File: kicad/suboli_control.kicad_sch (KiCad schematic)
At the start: 37 parts, among them SW1 DPST power switch panel header

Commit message: Review fixes R1: annotation, final values, TVS populated (SMBJ20A)
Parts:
- C11: value 220-470 uF / 25 V L output coupling -> 470uF/25V L output coupling
- C12: value 220-470 uF / 25 V R output coupling -> 470uF/25V R output coupling
- J1: renamed from J_DC; Function (none) -> DC barrel jack 5.5x2.5
- J2: renamed from J_IN; Function (none) -> 3.5 mm TRS input jack
- J3: renamed from J_SPK; Function (none) -> 4-pole Speakon/XLR tactile output
- J4: renamed from J_HP; Function (none) -> 3.5 mm TRS headphone output jack
- R2: value 47-100 k L input bias to VGND -> 100k L input bias to VGND
- R3: value 47-100 k R input bias to VGND -> 100k R input bias to VGND
- RV1: renamed from P_TACT; Function (none) -> Tactile volume, dual-gang 10k log
- RV2: renamed from P_HP; Function (none) -> Headphone volume, dual-gang 10k log
- TVS1: value SMBJ24A TVS -> SMBJ20A TVS; now fitted
- U1: renamed from U_vg; Function (none) -> Virtual ground rail splitter
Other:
- note added: "Headphone output is AC-coupled: J4 sleeve connects to GND_SIG, not VGND."
- note removed: "Headphone output is AC-coupled: J_HP sleeve connects to GND_SIG, not VGND."

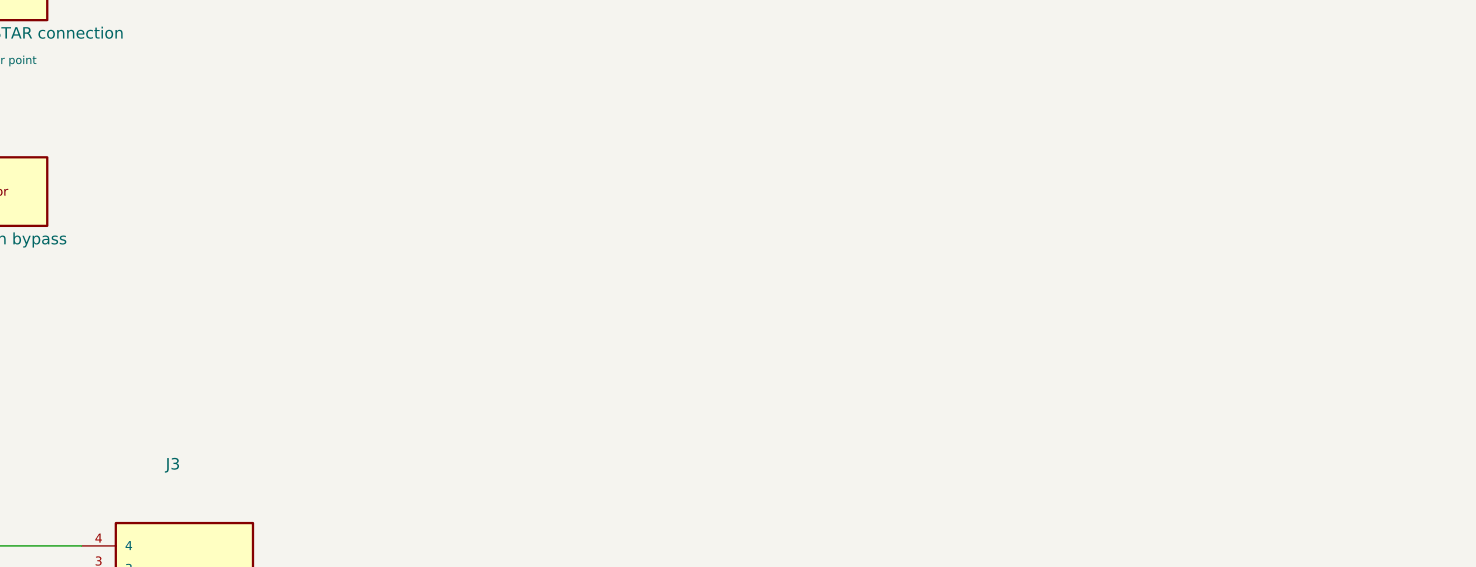
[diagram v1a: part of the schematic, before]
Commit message: R2: interior glow circuit, power-tracked via SW1
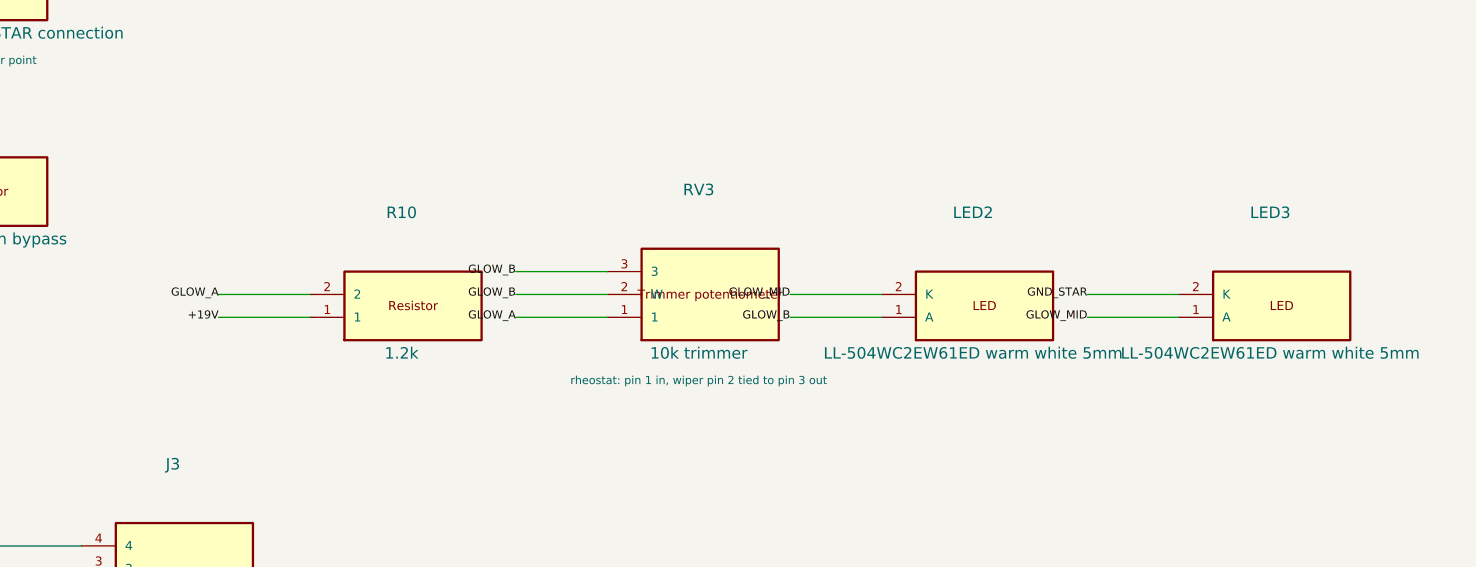
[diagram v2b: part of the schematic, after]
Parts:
- added LED2, LED3: LL-504WC2EW61ED warm white 5mm, symbol suboli_control:LED_2PIN
- added R10: 1.2k, symbol suboli_control:R_2PIN
- added RV3: 10k trimmer, symbol suboli_control:POT_3PIN
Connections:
- net +19V: now also R10.1
- net GND_STAR: now also LED3.2 (K)
- new net GLOW_A: R10.2, RV3.1
- new net GLOW_B: LED2.1 (A), RV3.2 (W), RV3.3
- new net GLOW_MID: LED2.2 (K), LED3.1 (A)
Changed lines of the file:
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@@
   (label "+19V_HP" (at 182.88 55.88 0) (effects (font (size 0.90 0.90)) (justify right)))
+  (symbol
+    (lib_id "suboli_control:R_2PIN")
+    (at 317.50 71.12 0)
+    (unit 1)
+    (exclude_from_sim no)
+    (in_bom yes)
+    (on_board yes)
+    (dnp no)
+    (property "Reference" "R10" (at 317.50 59.50 0) (effects (font (size 1.27 1.27))))
+    (property "Value" "1.2k" (at 317.50 75.12 0) (effects (font (size 1.27 1.27))))
+    (property "Footprint" "" (at 317.50 71.12 0) (effects (font (size 1.27 1.27)) (hide yes)))
+    (property "Datasheet" "~" (at 317.50 71.12 0) (effects (font (size 1.27 1.27)) (hide yes)))
+    (property "Function" "Glow current limit" (at 317.50 71.12 0) (effects (font (size 1.27 1.27)) (hide yes)))
+    (pin "1")
+    (pin "2")
+    (instances
+      (project "suboli_control"
+        (path "/35397207-27a9-5c6b-ad79-7b20c8370a7e"
+          (reference "R10")
+          (unit 1)
+        )
+      )
+    )
+  )
+  (wire (pts (xy 307.34 71.12) (xy 297.18 71.12)) (stroke (width 0) (type default)))
+  (label "+19V" (at 297.18 71.12 0) (effects (font (size 0.90 0.90)) (justify right)))
+  (wire (pts (xy 307.34 68.58) (xy 297.18 68.58)) (stroke (width 0) (type default)))
+  (label "GLOW_A" (at 297.18 68.58 0) (effects (font (size 0.90 0.90)) (justify right)))
+  (symbol
+    (lib_id "suboli_control:POT_3PIN")
+    (at 350.52 71.12 0)
+    (unit 1)
+    (exclude_from_sim no)
+    (in_bom yes)
+    (on_board yes)
+    (dnp no)
+    (property "Reference" "RV3" (at 350.52 56.96 0) (effects (font (size 1.27 1.27))))
+    (property "Value" "10k trimmer" (at 350.52 75.12 0) (effects (font (size 1.27 1.27))))
+    (property "Footprint" "" (at 350.52 71.12 0) (effects (font (size 1.27 1.27)) (hide yes)))
+    (property "Datasheet" "~" (at 350.52 71.12 0) (effects (font (size 1.27 1.27)) (hide yes)))
+    (property "Function" "Glow brightness set" (at 350.52 71.12 0) (effects (font (size 1.27 1.27)) (hide yes)))
+    (property "Wiring" "rheostat: pin 1 in, wiper pin 2 tied to pin 3 out" (at 350.52 78.12 0) (effects (font (size 0.90 0.90))))
+    (pin "1")
+    (pin "2")
+    (pin "3")
+    (instances
+      (project "suboli_control"
+        (path "/35397207-27a9-5c6b-ad79-7b20c8370a7e"
+          (reference "RV3")
+          (unit 1)
+        )
+      )
+    )
+  )
+  (wire (pts (xy 340.36 71.12) (xy 330.20 71.12)) (stroke (width 0) (type default)))
+  (label "GLOW_A" (at 330.20 71.12 0) (effects (font (size 0.90 0.90)) (justify right)))
+  (wire (pts (xy 340.36 68.58) (xy 330.20 68.58)) (stroke (width 0) (type default)))
+  (label "GLOW_B" (at 330.20 68.58 0) (effects (font (size 0.90 0.90)) (justify right)))
+  (wire (pts (xy 340.36 66.04) (xy 330.20 66.04)) (stroke (width 0) (type default)))
+  (label "GLOW_B" (at 330.20 66.04 0) (effects (font (size 0.90 0.90)) (justify right)))
+  (symbol
+    (lib_id "suboli_control:LED_2PIN")
+    (at 381.00 71.12 0)
+    (unit 1)
+    (exclude_from_sim no)
+    (in_bom yes)
+    (on_board yes)
+    (dnp no)
+    (property "Reference" "LED2" (at 381.00 59.50 0) (effects (font (size 1.27 1.27))))
+    (property "Value" "LL-504WC2EW61ED warm white 5mm" (at 381.00 75.12 0) (effects (font (size 1.27 1.27))))
+    (property "Footprint" "" (at 381.00 71.12 0) (effects (font (size 1.27 1.27)) (hide yes)))
+    (property "Datasheet" "~" (at 381.00 71.12 0) (effects (font (size 1.27 1.27)) (hide yes)))
+    (property "Function" "Interior glow" (at 381.00 71.12 0) (effects (font (size 1.27 1.27)) (hide yes)))
+    (pin "1")
+    (pin "2")
+    (instances
+      (project "suboli_control"
+        (path "/35397207-27a9-5c6b-ad79-7b20c8370a7e"
+          (reference "LED2")
+          (unit 1)
+        )
+      )
+    )
+  )
+  (wire (pts (xy 370.84 71.12) (xy 360.68 71.12)) (stroke (width 0) (type default)))
+  (label "GLOW_B" (at 360.68 71.12 0) (effects (font (size 0.90 0.90)) (justify right)))
+  (wire (pts (xy 370.84 68.58) (xy 360.68 68.58)) (stroke (width 0) (type default)))
+  (label "GLOW_MID" (at 360.68 68.58 0) (effects (font (size 0.90 0.90)) (justify right)))
+  (symbol
+    (lib_id "suboli_control:LED_2PIN")
+    (at 414.02 71.12 0)
+    (unit 1)
+    (exclude_from_sim no)
+    (in_bom yes)
+    (on_board yes)
+    (dnp no)
+    (property "Reference" "LED3" (at 414.02 59.50 0) (effects (font (size 1.27 1.27))))
+    (property "Value" "LL-504WC2EW61ED warm white 5mm" (at 414.02 75.12 0) (effects (font (size 1.27 1.27))))
+    (property "Footprint" "" (at 414.02 71.12 0) (effects (font (size 1.27 1.27)) (hide yes)))
+    (property "Datasheet" "~" (at 414.02 71.12 0) (effects (font (size 1.27 1.27)) (hide yes)))
+    (property "Function" "Interior glow" (at 414.02 71.12 0) (effects (font (size 1.27 1.27)) (hide yes)))
+    (pin "1")
+    (pin "2")
+    (instances
+      (project "suboli_control"
+        (path "/35397207-27a9-5c6b-ad79-7b20c8370a7e"
+          (reference "LED3")
+          (unit 1)
+        )
+      )
+    )
+  )
+  (wire (pts (xy 403.86 71.12) (xy 393.70 71.12)) (stroke (width 0) (type default)))
+  (label "GLOW_MID" (at 393.70 71.12 0) (effects (font (size 0.90 0.90)) (justify right)))
+  (wire (pts (xy 403.86 68.58) (xy 393.70 68.58)) (stroke (width 0) (type default)))
+  (label "GND_STAR" (at 393.70 68.58 0) (effects (font (size 0.90 0.90)) (justify right)))
   (symbol
     (lib_id "suboli_control:CONN_3_TRS")

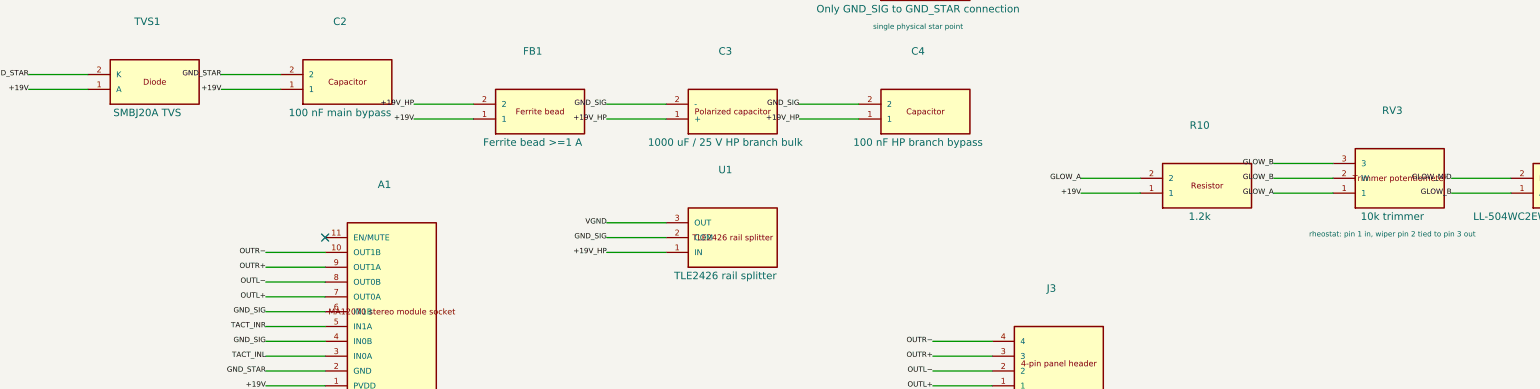
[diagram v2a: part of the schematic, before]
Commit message: R3: footprints locked from verified parts, TVS=P6KE24A, script archived
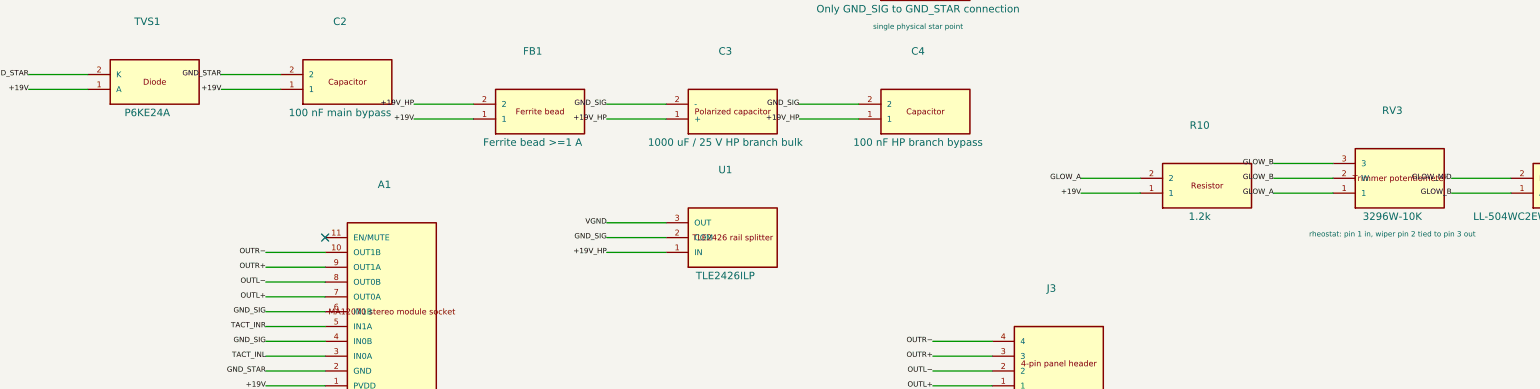
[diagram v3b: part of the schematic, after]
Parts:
- A2: footprint (none) -> Package_DIP:DIP-8_W7.62mm_Socket; Supplier (none) -> HESTORE; Supplier_PN (none) -> 100.231.43
- C1: footprint (none) -> Capacitor_THT:CP_Radial_D12.5mm_P5.00mm; Supplier (none) -> HESTORE; Supplier_PN (none) -> 100.432.81
- C10, C9: footprint (none) -> Capacitor_THT:C_Rect_L7.2mm_W4.5mm_P5.00mm; Supplier (none) -> HESTORE; Supplier_PN (none) -> 100.008.95
- C11, C12: footprint (none) -> Capacitor_THT:CP_Radial_D10.0mm_P5.00mm; Supplier (none) -> HESTORE; Supplier_PN (none) -> 100.285.01
- C2, C4, C7, C8: footprint (none) -> Capacitor_THT:C_Disc_D7.5mm_W4.4mm_P5.00mm; Supplier (none) -> HESTORE; Supplier_PN (none) -> 100.448.15
- C3: footprint (none) -> Capacitor_THT:CP_Radial_D10.0mm_P5.00mm; Supplier (none) -> HESTORE; Supplier_PN (none) -> 100.310.10
- C5, C6: footprint (none) -> Capacitor_THT:CP_Radial_D5.0mm_P2.00mm; Supplier (none) -> HESTORE; Supplier_PN (none) -> 100.004.04
- D1: footprint (none) -> Diode_THT:D_DO-201AD_P15.24mm_Horizontal; Supplier (none) -> HESTORE; Supplier_PN (none) -> 100.492.21
- F1: footprint (none) -> suboli_control:PPTC_LP30-300_P7.60mm; Supplier (none) -> HESTORE; Supplier_PN (none) -> 100.238.56
- FB1: footprint (none) -> Inductor_THT:L_Axial_L12.0mm_D5.0mm_P15.24mm_Horizontal; Supplier (none) -> HESTORE; Supplier_PN (none) -> 100.358.61
- J1: footprint (none) -> TerminalBlock_Phoenix:TerminalBlock_Phoenix_MSTBA-2,5_1x02_P5.08mm_Horizontal; Supplier (none) -> HESTORE; Supplier_PN (none) -> 100.425.38
- J2, J4: footprint (none) -> Connector_JST:JST_XH_B3B-XH-A_1x03_P2.50mm_Vertical; Supplier (none) -> HESTORE; Supplier_PN (none) -> 100.415.50
- J3, SW1: footprint (none) -> TerminalBlock_Phoenix:TerminalBlock_Phoenix_MSTBA-2,5_1x04_P5.08mm_Horizontal; Supplier (none) -> HESTORE; Supplier_PN (none) -> 100.425.40
- LED1: footprint (none) -> LED_THT:LED_D5.0mm; Supplier (none) -> HESTORE
- LED2, LED3: footprint (none) -> LED_THT:LED_D5.0mm; Supplier (none) -> HESTORE; Supplier_PN (none) -> 100.392.63
- NT1: footprint (none) -> NetTie:NetTie-2_SMD_Pad0.5mm; Supplier (none) -> HESTORE
- R1: footprint (none) -> Resistor_THT:R_Axial_DIN0207_L6.3mm_D2.5mm_P10.16mm_Horizontal; Supplier (none) -> HESTORE; Supplier_PN (none) -> 100.205.39
- R10: footprint (none) -> Resistor_THT:R_Axial_DIN0207_L6.3mm_D2.5mm_P10.16mm_Horizontal; Supplier (none) -> HESTORE; Supplier_PN (none) -> 100.205.19
- R2, R3: footprint (none) -> Resistor_THT:R_Axial_DIN0207_L6.3mm_D2.5mm_P10.16mm_Horizontal; Supplier (none) -> HESTORE; Supplier_PN (none) -> 100.205.64
- R4, R5, R6, R7: footprint (none) -> Resistor_THT:R_Axial_DIN0207_L6.3mm_D2.5mm_P10.16mm_Horizontal; Supplier (none) -> HESTORE; Supplier_PN (none) -> 100.205.41
- R8, R9: footprint (none) -> Resistor_THT:R_Axial_DIN0207_L6.3mm_D2.5mm_P10.16mm_Horizontal; Supplier (none) -> HESTORE; Supplier_PN (none) -> 100.204.73
- RV1, RV2: footprint (none) -> Connector_JST:JST_XH_B6B-XH-A_1x06_P2.50mm_Vertical; Supplier (none) -> HESTORE
- RV3: value 10k trimmer -> 3296W-10K; footprint (none) -> Potentiometer_THT:Potentiometer_Bourns_3296W_Vertical; Supplier (none) -> HESTORE
- TVS1: value SMBJ20A TVS -> P6KE24A; footprint (none) -> Diode_THT:D_DO-15_P10.16mm_Horizontal; Supplier (none) -> HESTORE
- U1: value TLE2426 rail splitter -> TLE2426ILP; footprint (none) -> Package_TO_SOT_THT:TO-92_Inline; Supplier (none) -> HESTORE

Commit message: R3.1: correct 3 footprint library names (MSTB pluggable lib, Fastron suffix)
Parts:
- FB1: footprint Inductor_THT:L_Axial_L12.0mm_D5.0mm_P15.24mm_Horizontal -> Inductor_THT:L_Axial_L12.0mm_D5.0mm_P15.24mm_Horizontal_Fastron_MISC
- J1: footprint TerminalBlock_Phoenix:TerminalBlock_Phoenix_MSTBA-2,5_1x02_P5.08mm_Horizontal -> Connector_Phoenix_MSTB:PhoenixContact_MSTBA_2,5_2-G-5,08_1x02_P5.08mm_Horizontal
- J3, SW1: footprint TerminalBlock_Phoenix:TerminalBlock_Phoenix_MSTBA-2,5_1x04_P5.08mm_Horizontal -> Connector_Phoenix_MSTB:PhoenixContact_MSTBA_2,5_4-G-5,08_1x04_P5.08mm_Horizontal
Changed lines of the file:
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@@
     (property "Reference" "J1" (at 27.94 21.40 0) (effects (font (size 1.27 1.27))))
     (property "Value" "DC barrel jack panel header 5.5x2.5" (at 27.94 37.02 0) (effects (font (size 1.27 1.27))))
-    (property "Footprint" "TerminalBlock_Phoenix:TerminalBlock_Phoenix_MSTBA-2,5_1x02_P5.08mm_Horizontal" (at 27.94 33.02 0) (effects (font (size 1.27 1.27)) (hide yes)))
+    (property "Footprint" "Connector_Phoenix_MSTB:PhoenixContact_MSTBA_2,5_2-G-5,08_1x02_P5.08mm_Horizontal" (at 27.94 33.02 0) (effects (font (size 1.27 1.27)) (hide yes)))
     (property "Datasheet" "~" (at 27.94 33.02 0) (effects (font (size 1.27 1.27)) (hide yes)))
     (property "Supplier" "HESTORE" (at 27.94 33.02 0) (effects (font (size 1.27 1.27)) (hide yes)))
@@
     (property "Reference" "SW1" (at 68.58 18.86 0) (effects (font (size 1.27 1.27))))
     (property "Value" "DPST power switch panel header" (at 68.58 39.56 0) (effects (font (size 1.27 1.27))))
-    (property "Footprint" "TerminalBlock_Phoenix:TerminalBlock_Phoenix_MSTBA-2,5_1x04_P5.08mm_Horizontal" (at 68.58 35.56 0) (effects (font (size 1.27 1.27)) (hide yes)))
+    (property "Footprint" "Connector_Phoenix_MSTB:PhoenixContact_MSTBA_2,5_4-G-5,08_1x04_P5.08mm_Horizontal" (at 68.58 35.56 0) (effects (font (size 1.27 1.27)) (hide yes)))
     (property "Datasheet" "~" (at 68.58 35.56 0) (effects (font (size 1.27 1.27)) (hide yes)))
     (property "Supplier" "HESTORE" (at 68.58 35.56 0) (effects (font (size 1.27 1.27)) (hide yes)))
@@
     (property "Reference" "FB1" (at 203.20 46.80 0) (effects (font (size 1.27 1.27))))
     (property "Value" "Ferrite bead >=1 A" (at 203.20 62.42 0) (effects (font (size 1.27 1.27))))
-    (property "Footprint" "Inductor_THT:L_Axial_L12.0mm_D5.0mm_P15.24mm_Horizontal" (at 203.20 58.42 0) (effects (font (size 1.27 1.27)) (hide yes)))
+    (property "Footprint" "Inductor_THT:L_Axial_L12.0mm_D5.0mm_P15.24mm_Horizontal_Fastron_MISC" (at 203.20 58.42 0) (effects (font (size 1.27 1.27)) (hide yes)))
     (property "Datasheet" "~" (at 203.20 58.42 0) (effects (font (size 1.27 1.27)) (hide yes)))
     (property "Supplier" "HESTORE" (at 203.20 58.42 0) (effects (font (size 1.27 1.27)) (hide yes)))
@@
     (property "Reference" "J3" (at 292.10 87.44 0) (effects (font (size 1.27 1.27))))
     (property "Value" "4-pole Speakon/XLR panel header" (at 292.10 108.14 0) (effects (font (size 1.27 1.27))))
-    (property "Footprint" "TerminalBlock_Phoenix:TerminalBlock_Phoenix_MSTBA-2,5_1x04_P5.08mm_Horizontal" (at 292.10 104.14 0) (effects (font (size 1.27 1.27)) (hide yes)))
+    (property "Footprint" "Connector_Phoenix_MSTB:PhoenixContact_MSTBA_2,5_4-G-5,08_1x04_P5.08mm_Horizontal" (at 292.10 104.14 0) (effects (font (size 1.27 1.27)) (hide yes)))
     (property "Datasheet" "~" (at 292.10 104.14 0) (effects (font (size 1.27 1.27)) (hide yes)))
     (property "Supplier" "HESTORE" (at 292.10 104.14 0) (effects (font (size 1.27 1.27)) (hide yes)))
